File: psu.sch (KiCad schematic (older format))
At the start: 23 parts, among them J401 USB_C_Receptacle_USB2.0, U401 LTC3622*DE

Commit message: Major work on the power supply: - Swapped the input filter inductor for a significantly smaller one - Basically finished laying out the switching supply
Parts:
- L401: footprint Inductor_SMD:L_Bourns_SRR1210A -> myfp:L_Panasonic_ETQ-P4MxxxKFM; Part# SRR1210-470M -> ETQ-P4M470KFM
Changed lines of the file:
@@
 F 0 "L401" V 6640 1200 50  0000 C CNN
 F 1 "47uH" V 6549 1200 50  0000 C CNN
-F 2 "Inductor_SMD:L_Bourns_SRR1210A" H 6450 1200 50  0001 C CNN
+F 2 "myfp:L_Panasonic_ETQ-P4MxxxKFM" H 6450 1200 50  0001 C CNN
 F 3 "~" H 6450 1200 50  0001 C CNN
 F 4 ">3.0A" V 6450 1200 50  0001 C CNN "Isat"
-F 5 "SRR1210-470M" V 6450 1200 50  0001 C CNN "Part#"
+F 5 "ETQ-P4M470KFM" V 6450 1200 50  0001 C CNN "Part#"
 	1    6450 1200
 	0    -1   -1   0

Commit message: Exported schematic PDF and BoM, the latter manually massaged. Added a couple missing part #s for big things which seemed important.
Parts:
- J401: Part# (none) -> USB4085-GF-A
- U401: Part# (none) -> LTC3622IDE#PBF
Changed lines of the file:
@@
 F 2 "myfp:USB_C_GCT_USB4085" H 2150 2000 50  0001 C CNN
 F 3 "https://www.usb.org/sites/default/files/documents/usb_type-c.zip" H 2150 2000 50  0001 C CNN
+F 4 "USB4085-GF-A" H 2000 2000 50  0001 C CNN "Part#"
 	1    2000 2000
 	1    0    0    -1
@@
 F 2 "Package_DFN_QFN:DFN-14-1EP_3x4mm_P0.5mm_EP1.7x3.3mm" H 9000 2850 50  0001 C CNN
 F 3 "" H 9000 2000 50  0001 C CNN
+F 4 "LTC3622IDE#PBF" H 9000 2000 50  0001 C CNN "Part#"
 	1    9000 2000
 	1    0    0    -1

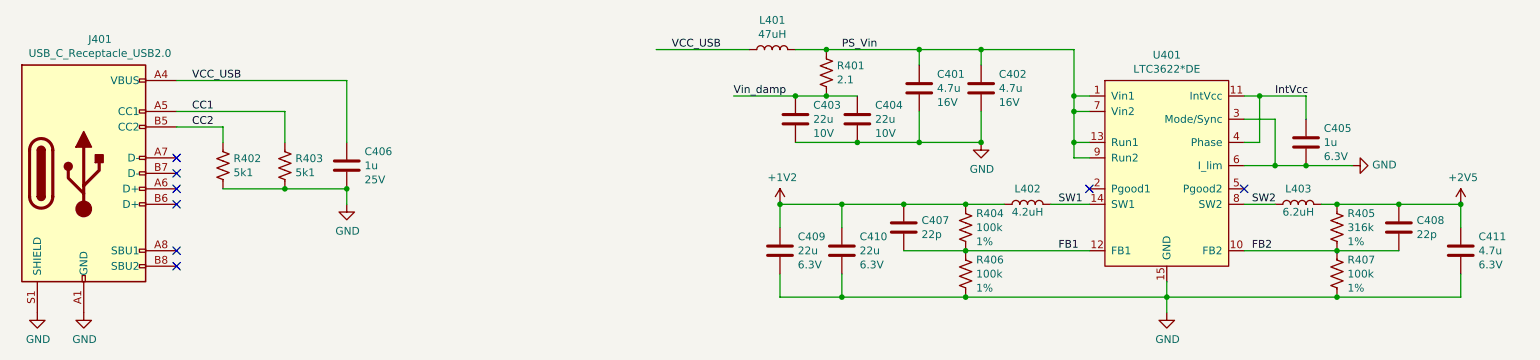
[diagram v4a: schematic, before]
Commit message: Forward progress: - Ripped up a good chunk of the old place&route around the PHYs - Swizzled graphical placement of LAN8831 diff pair pins, to make the trace   routing be straight-thru.  This also involved swapping the polarity I'm   feeding into the magnetics.  Bonus: the magnetics-to-RJ45 is now straight,   instead of having to go around the back sides! - Adjusted some default trace spacings because of the tiny 0.4mm QFN:   - Switched default traces from 8mil to 7.8mil   - Switched diff pairs from 8.8/8.1 to 7.4/7.8 - Whoops, not all the 0.1uF decoupling caps were 0402 sized yet - Filled in a lot of specific vendor P/Ns for resistors & capacitors, to make   dealing with assembly houses easier
PHY1 has all its close-in decoupling caps placed & routed, PHY2 does not yet.
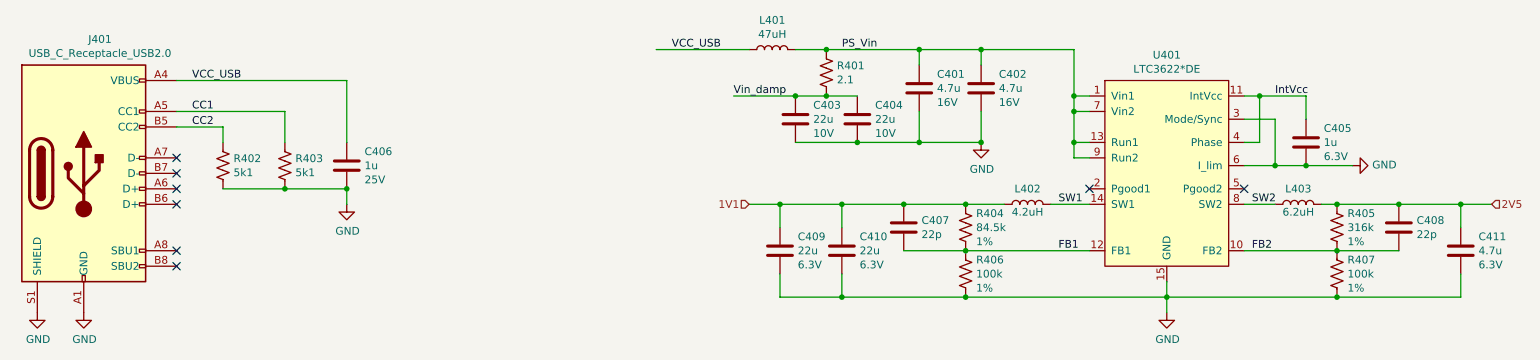
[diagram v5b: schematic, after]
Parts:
- R402, R403: Part# (none) -> ERJ-3EKF5101V
- R404: value 100k -> 84.5k; Part# (none) -> ERJ-3EKF8452V
- R405: Part# (none) -> ERJ-3EKF3163V
- R406, R407: Part# (none) -> ERJ-3EKF1003V
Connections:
- net +1V2 renamed 1V1
- net +2V5 renamed 2V5
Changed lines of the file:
@@
 $EndComp
 $Comp
-L power:GND #PWR0407
+L power:GND #PWR0405
 U 1 1 63923FD7
 P 2000 2900
-F 0 "#PWR0407" H 2000 2650 50  0001 C CNN
+F 0 "#PWR0405" H 2000 2650 50  0001 C CNN
 F 1 "GND" H 2005 2727 50  0000 C CNN
 F 2 "" H 2000 2900 50  0001 C CNN
@@
 $EndComp
 $Comp
-L power:GND #PWR0406
+L power:GND #PWR0404
 U 1 1 63923FFC
 P 1700 2900
-F 0 "#PWR0406" H 1700 2650 50  0001 C CNN
+F 0 "#PWR0404" H 1700 2650 50  0001 C CNN
 F 1 "GND" H 1705 2727 50  0000 C CNN
 F 2 "" H 1700 2900 50  0001 C CNN
@@
 F 2 "Resistor_SMD:R_0603_1608Metric" V 2940 1940 50  0001 C CNN
 F 3 "~" H 2900 1950 50  0001 C CNN
+F 4 "ERJ-3EKF5101V" H 0   0   50  0001 C CNN "Part#"
 	1    2900 1950
 	1    0    0    -1
@@
 F 2 "Resistor_SMD:R_0603_1608Metric" V 3340 1940 50  0001 C CNN
 F 3 "~" H 3300 1950 50  0001 C CNN
+F 4 "ERJ-3EKF5101V" H 0   0   50  0001 C CNN "Part#"
 	1    3300 1950
 	1    0    0    -1
@@
 $EndComp
 $Comp
-L power:GND #PWR0408
+L power:GND #PWR0406
 U 1 1 639285B5
 P 9000 2900
-F 0 "#PWR0408" H 9000 2650 50  0001 C CNN
+F 0 "#PWR0406" H 9000 2650 50  0001 C CNN
 F 1 "GND" H 9005 2727 50  0000 C CNN
 F 2 "" H 9000 2900 50  0001 C CNN
@@
 P 7700 2350
 F 0 "R404" H 7768 2441 50  0000 L CNN
-F 1 "100k" H 7768 2350 50  0000 L CNN
+F 1 "84.5k" H 7768 2350 50  0000 L CNN
 F 2 "Resistor_SMD:R_0603_1608Metric" V 7740 2340 50  0001 C CNN
 F 3 "~" H 7700 2350 50  0001 C CNN
 F 4 "1%" H 7768 2259 50  0000 L CNN "Tolerance"
+F 5 "ERJ-3EKF8452V" H 7700 2350 50  0001 C CNN "Part#"
 	1    7700 2350
 	1    0    0    -1
@@
 F 3 "~" H 7700 2650 50  0001 C CNN
 F 4 "1%" H 7768 2559 50  0000 L CNN "Tolerance"
+F 5 "ERJ-3EKF1003V" H 0   0   50  0001 C CNN "Part#"
 	1    7700 2650
 	1    0    0    -1
@@
 Wire Wire Line
 	6900 2200 6900 2350
-$Comp
-L power:+1V2 #PWR0404
-U 1 1 6392CD5B
-P 6500 2200
-F 0 "#PWR0404" H 6500 2050 50  0001 C CNN
-F 1 "+1V2" H 6515 2373 50  0000 C CNN
-F 2 "" H 6500 2200 50  0001 C CNN
-F 3 "" H 6500 2200 50  0001 C CNN
-	1    6500 2200
-	1    0    0    -1
-$EndComp
 Connection ~ 6900 2200
 $Comp
@@
 F 3 "~" H 10100 2350 50  0001 C CNN
 F 4 "1%" H 10168 2259 50  0000 L CNN "Tolerance"
+F 5 "ERJ-3EKF3163V" H 0   0   50  0001 C CNN "Part#"
 	1    10100 2350
 	1    0    0    -1
@@
 F 3 "~" H 10100 2650 50  0001 C CNN
 F 4 "1%" H 10168 2559 50  0000 L CNN "Tolerance"
+F 5 "ERJ-3EKF1003V" H 0   0   50  0001 C CNN "Part#"
 	1    10100 2650
 	1    0    0    -1
@@
 	10500 2200 10900 2200
 Connection ~ 10500 2200
-$Comp
-L power:+2V5 #PWR0405
-U 1 1 639329DA
-P 10900 2200
-F 0 "#PWR0405" H 10900 2050 50  0001 C CNN
-F 1 "+2V5" H 10915 2373 50  0000 C CNN
-F 2 "" H 10900 2200 50  0001 C CNN
-F 3 "" H 10900 2200 50  0001 C CNN
-	1    10900 2200
-	1    0    0    -1
-$EndComp
-Connection ~ 10900 2200
 Wire Wire Line
 	10000 2200 10100 2200
@@
 Wire Wire Line
 	6500 2200 6500 2350
-Connection ~ 6500 2200
 Wire Wire Line
 	6500 2650 6500 2800
@@
 Wire Wire Line
 	7700 2800 9000 2800
+Text HLabel 11100 2200 2    50   Input ~ 0
+2V5
+Wire Wire Line
+	11100 2200 10900 2200
+Connection ~ 10900 2200
+Wire Wire Line
+	6500 2200 6300 2200
+Connection ~ 6500 2200
+Text HLabel 6300 2200 0    50   Input ~ 0
+1V1
 $EndSCHEMATC

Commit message: - Sanitized some of the capacitor voltages / footprints - Selected mfr P/Ns for *all* parts - Placed and routed most of the series resistors, ran into a problem with the   VDD vias on PHY1..... - Placed and routed (all?) the bypass caps for PHY2
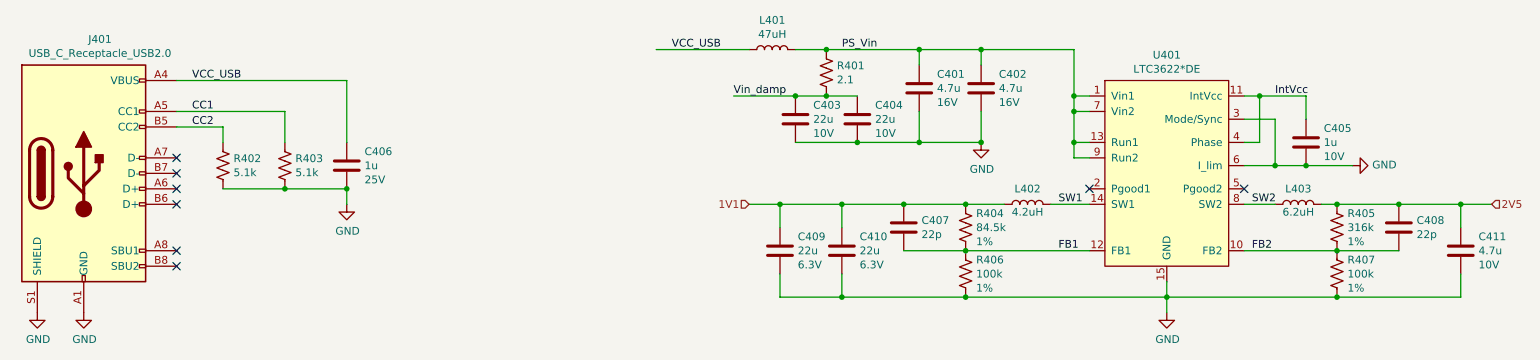
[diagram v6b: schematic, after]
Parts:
- C401, C402: Part# (none) -> CGA4J3X7R1C475M125AB
- C403, C404: Part# (none) -> GCJ31CR71A226KE01K
- C405: Part# (none) -> CGA3E1X7R1E105K080AC; Voltage 6.3V -> 10V
- C406: Part# (none) -> CGA3E1X7R1E105K080AC
- C407, C408: Part# (none) -> CGA3E2NP01H220J080AA
- C409, C410: Part# (none) -> CGA5L1X7R0J226M160AC
- C411: Part# (none) -> CGA4J3X7R1C475M125AB; Voltage 6.3V -> 10V
- R401: Part# (none) -> ERJ-3GEYJ2R2V
- R402, R403: value 5k1 -> 5.1k
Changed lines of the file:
@@
 P 2900 1950
 F 0 "R402" H 2968 1996 50  0000 L CNN
-F 1 "5k1" H 2968 1905 50  0000 L CNN
+F 1 "5.1k" H 2968 1905 50  0000 L CNN
 F 2 "Resistor_SMD:R_0603_1608Metric" V 2940 1940 50  0001 C CNN
 F 3 "~" H 2900 1950 50  0001 C CNN
@@
 P 3300 1950
 F 0 "R403" H 3368 1996 50  0000 L CNN
-F 1 "5k1" H 3368 1905 50  0000 L CNN
+F 1 "5.1k" H 3368 1905 50  0000 L CNN
 F 2 "Resistor_SMD:R_0603_1608Metric" V 3340 1940 50  0001 C CNN
 F 3 "~" H 3300 1950 50  0001 C CNN
@@
 F 3 "~" H 3700 1950 50  0001 C CNN
 F 4 "25V" H 3815 1859 50  0000 L CNN "Voltage"
+F 5 "CGA3E1X7R1E105K080AC" H 0   0   50  0001 C CNN "Part#"
 	1    3700 1950
 	1    0    0    -1
@@
 F 2 "Capacitor_SMD:C_0603_1608Metric" H 9938 1650 50  0001 C CNN
 F 3 "~" H 9900 1800 50  0001 C CNN
-F 4 "6.3V" H 10015 1709 50  0000 L CNN "Voltage"
+F 4 "10V" H 10015 1709 50  0000 L CNN "Voltage"
+F 5 "CGA3E1X7R1E105K080AC" H 0   0   50  0001 C CNN "Part#"
 	1    9900 1800
 	1    0    0    -1
@@
 F 2 "Capacitor_SMD:C_0603_1608Metric" H 7338 2200 50  0001 C CNN
 F 3 "~" H 7300 2350 50  0001 C CNN
+F 4 "CGA3E2NP01H220J080AA" H 0   0   50  0001 C CNN "Part#"
 	1    7300 2350
 	1    0    0    -1
@@
 F 3 "~" H 6900 2500 50  0001 C CNN
 F 4 "6.3V" H 7015 2409 50  0000 L CNN "Voltage"
+F 5 "CGA5L1X7R0J226M160AC" H 0   0   50  0001 C CNN "Part#"
 	1    6900 2500
 	1    0    0    -1
@@
 F 2 "Capacitor_SMD:C_0603_1608Metric" H 10538 2200 50  0001 C CNN
 F 3 "~" H 10500 2350 50  0001 C CNN
+F 4 "CGA3E2NP01H220J080AA" H 0   0   50  0001 C CNN "Part#"
 	1    10500 2350
 	1    0    0    -1
@@
 F 2 "Capacitor_SMD:C_0805_2012Metric" H 10938 2350 50  0001 C CNN
 F 3 "~" H 10900 2500 50  0001 C CNN
-F 4 "6.3V" H 11015 2409 50  0000 L CNN "Voltage"
+F 4 "10V" H 11015 2409 50  0000 L CNN "Voltage"
+F 5 "CGA4J3X7R1C475M125AB" H 0   0   50  0001 C CNN "Part#"
 	1    10900 2500
 	1    0    0    -1
@@
 F 3 "~" H 6500 2500 50  0001 C CNN
 F 4 "6.3V" H 6615 2409 50  0000 L CNN "Voltage"
+F 5 "CGA5L1X7R0J226M160AC" H 0   0   50  0001 C CNN "Part#"
 	1    6500 2500
 	1    0    0    -1
@@
 F 3 "~" H 7400 1450 50  0001 C CNN
 F 4 "16V" H 7515 1359 50  0000 L CNN "Voltage"
+F 5 "CGA4J3X7R1C475M125AB" H 0   0   50  0001 C CNN "Part#"
 	1    7400 1450
 	1    0    0    -1
@@
 F 3 "~" H 7000 1650 50  0001 C CNN
 F 4 "10V" H 7115 1559 50  0000 L CNN "Voltage"
+F 5 "GCJ31CR71A226KE01K" H 0   0   50  0001 C CNN "Part#"
 	1    7000 1650
 	1    0    0    -1
@@
 F 3 "~" H 6600 1650 50  0001 C CNN
 F 4 "10V" H 6715 1559 50  0000 L CNN "Voltage"
+F 5 "GCJ31CR71A226KE01K" H 0   0   50  0001 C CNN "Part#"
 	1    6600 1650
 	1    0    0    -1
@@
 F 2 "Resistor_SMD:R_0603_1608Metric" V 6840 1340 50  0001 C CNN
 F 3 "~" H 6800 1350 50  0001 C CNN
+F 4 "ERJ-3GEYJ2R2V" H 0   0   50  0001 C CNN "Part#"
 	1    6800 1350
 	1    0    0    -1
@@
 F 3 "~" H 7800 1450 50  0001 C CNN
 F 4 "16V" H 7915 1359 50  0000 L CNN "Voltage"
+F 5 "CGA4J3X7R1C475M125AB" H 0   0   50  0001 C CNN "Part#"
 	1    7800 1450
 	1    0    0    -1
